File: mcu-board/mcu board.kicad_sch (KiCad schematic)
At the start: 1 part, among them U1 ESP32-S3-1

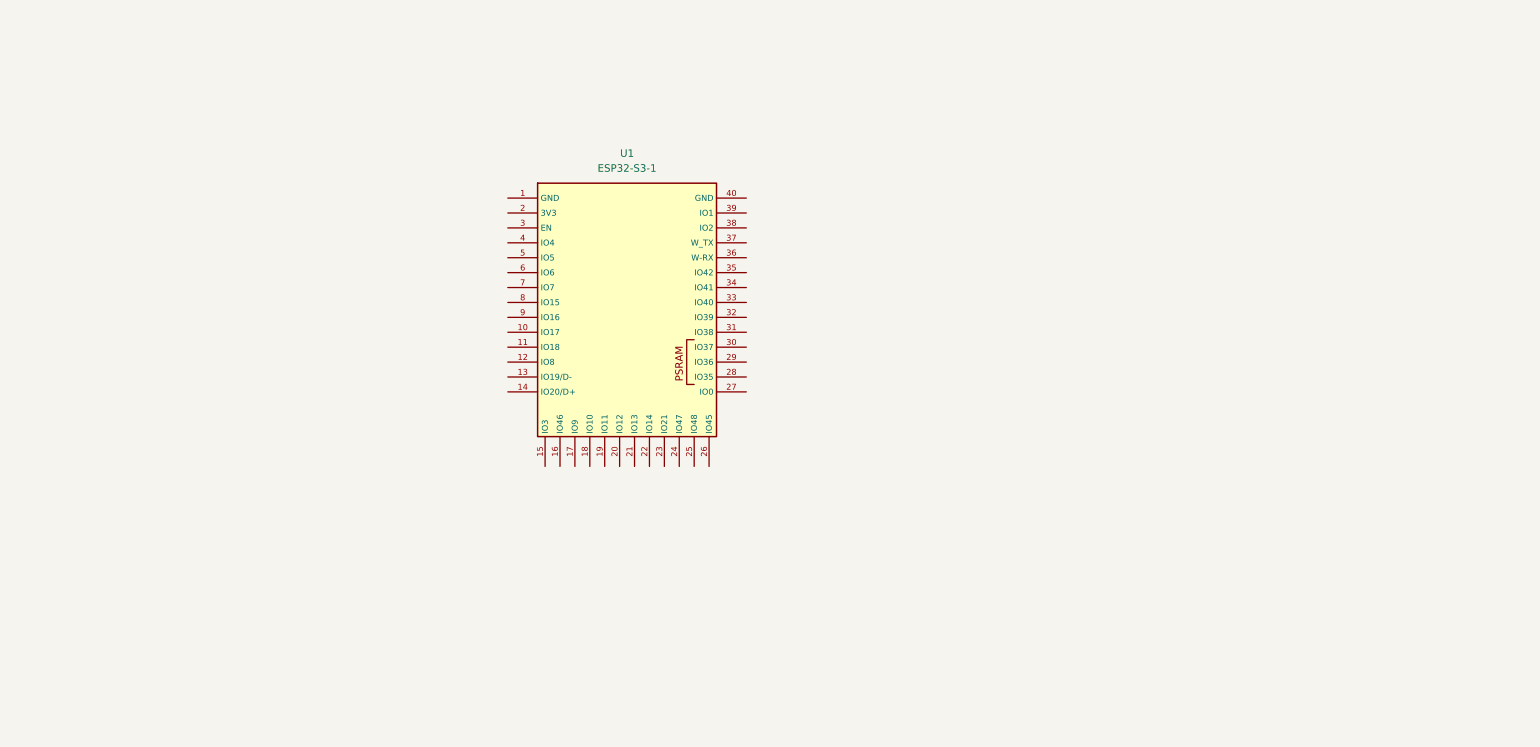
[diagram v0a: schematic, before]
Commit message: added usb-c, power, started on mcu
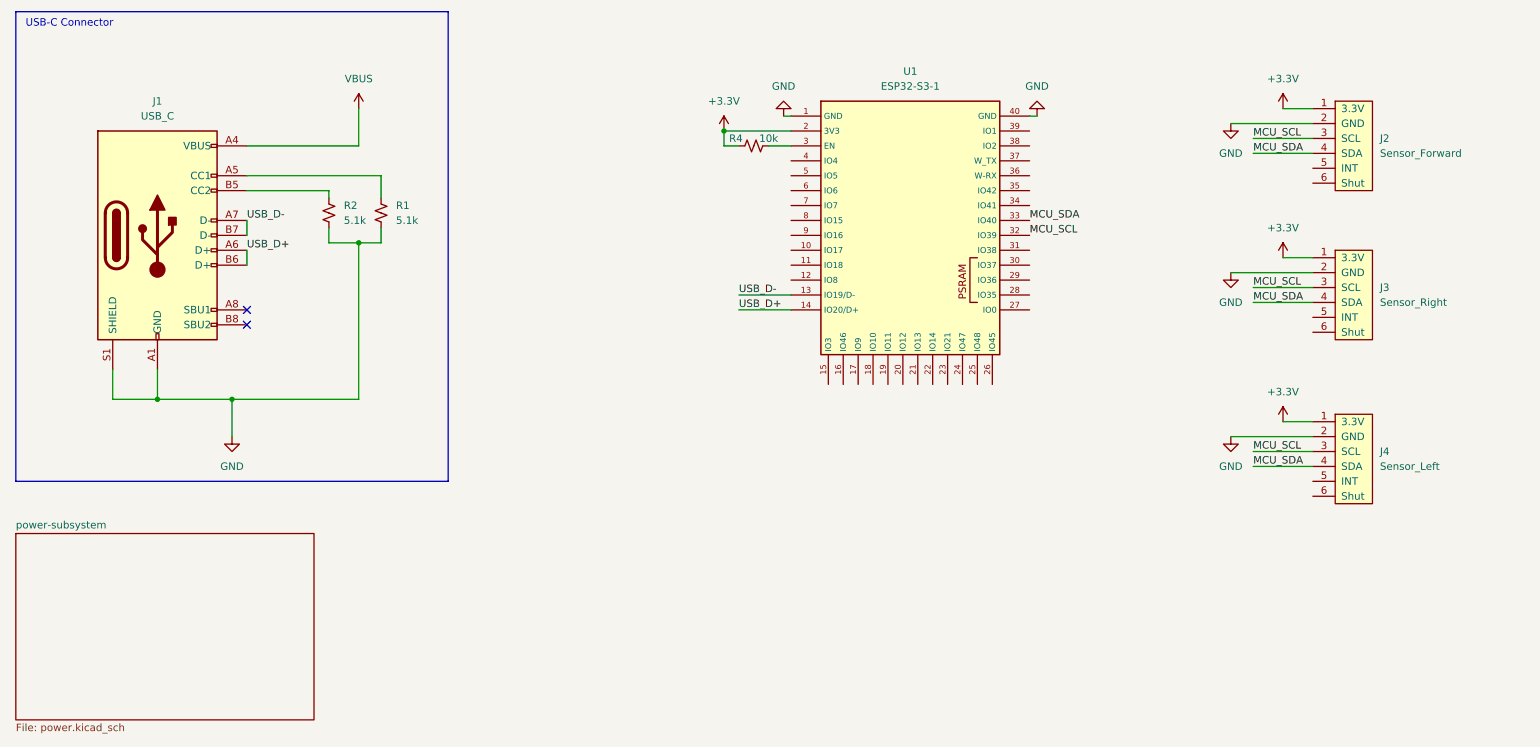
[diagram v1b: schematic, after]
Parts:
- added J1: USB_C, symbol Connector:USB_C_Receptacle_USB2.0_16P
- added J2: Sensor_Forward, EESD:1x6 Socket, symbol mouseLib:TofF breakout
- added J3: Sensor_Right, EESD:1x6 Socket, symbol mouseLib:TofF breakout
- added J4: Sensor_Left, EESD:1x6 Socket, symbol mouseLib:TofF breakout
- added R1, R2: 5.1k, symbol Device:R_Small_US
- added R4: 10k, symbol Device:R_Small_US
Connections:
- net GND: now reaches U1.1 (GND)
- net GND: now also U1.40 (GND), U1.41 (GND__1), J1.A1 (GND), J1.A12 (GND), J1.B1 (GND), J1.B12 (GND), J1.S1 (SHIELD), J2.2 (GND), J3.2 (GND), J4.2 (GND), R1.1, R2.1
- net USB_D-: now reaches U1.13 (IO19/D-)
- net USB_D-: now also J1.A7 (D-), J1.B7 (D-)
- net USB_D+: now reaches U1.14 (IO20/D+)
- net USB_D+: now also J1.A6 (D+), J1.B6 (D+)
- net +3.3V: now reaches U1.2 (3V3)
- net +3.3V: now also J2.1 (3.3V), J3.1 (3.3V), J4.1 (3.3V), R4.1
- net at U1.3 (EN): now also R4.2
- net MCU_SCL: now reaches U1.32 (IO39)
- net MCU_SCL: now also J2.3 (SCL), J3.3 (SCL), J4.3 (SCL)
- net MCU_SDA: now reaches U1.33 (IO40)
- net MCU_SDA: now also J2.4 (SDA), J3.4 (SDA), J4.4 (SDA)
- new net: J1.A5 (CC1), R1.2
- new net: J1.B5 (CC2), R2.2
- new net VBUS: J1.A4 (VBUS), J1.A9 (VBUS), J1.B4 (VBUS), J1.B9 (VBUS)
- no-connect marks 0 -> 2
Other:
- added sheet power-subsystem (power.kicad_sch)
- note added: "USB-C Connector"
- company: (none) -> Team 6.7 MHz
- title: (none) -> Mouse Board
- moved on the sheet: U1

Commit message: finished schematic(?)
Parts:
- added C7: .1u, symbol Device:C_Small
- added C8: 1u, symbol Device:C_Small
- added C9: 22u, symbol Device:C_Small
- added D4: LED, symbol Device:LED
- added J5: I2C Breakout, symbol Connector_Generic:Conn_01x04
- added M1, M2: ~, RMSmouse:gearmotorenc, symbol mouseLib:Motor
- added SW1: BOOT, symbol Switch:SW_Push
- added SW2: RESET, symbol Switch:SW_Push
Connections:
- net +3.3V: now also R4.2, C9.2, J5.2 (Pin_2); no longer R4.1
- net GND: now also C7.2, C8.2, C9.1, D4.1 (K), J5.1 (Pin_1), SW1.2, SW2.2
- net MCU_SCL: now also J5.3 (Pin_3)
- net MCU_SDA: now also J5.4 (Pin_4)
- net MCU_ENABLE: now reaches U1.3 (EN)
- net MCU_ENABLE: now also R4.1, C8.1, SW2.1; no longer R4.2
- net MCU_IO17: now reaches U1.10 (IO17)
- net MCU_IO17: now also J4.5 (INT)
- net BOOT_SEL: now reaches U1.27 (IO0)
- net BOOT_SEL: now also C7.1, SW1.1
- net at U1.35 (IO42): now also D4.2 (A)
- net MCU_IO4: now reaches U1.4 (IO4)
- net MCU_IO4: now also J4.6 (Shut)
- net MCU_IO6: now reaches U1.6 (IO6)
- net MCU_IO6: now also J2.6 (Shut)
- net MCU_IO7: now reaches U1.7 (IO7)
- net MCU_IO7: now also J3.6 (Shut)
- net MCU_IO15: now reaches U1.8 (IO15)
- net MCU_IO15: now also J2.5 (INT)
- net MCU_IO16: now reaches U1.9 (IO16)
- net MCU_IO16: now also J3.5 (INT)
- no-connect marks 2 -> 3
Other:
- note added: "blinky for testing mcu"
- moved on the sheet: J2, J3, J4, R4

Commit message: footprints
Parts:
- C7, C8: footprint (none) -> Capacitor_SMD:C_0603_1608Metric
- C9: footprint (none) -> Capacitor_SMD:C_0805_2012Metric
- J1: footprint (none) -> Connector_USB:USB_C_Receptacle_GCT_USB4105-xx-A_16P_TopMnt_Horizontal
- J5: footprint (none) -> Connector_PinSocket_2.54mm:PinSocket_1x40_P2.54mm_Vertical
- M1, M2: footprint RMSmouse:gearmotorenc -> mouseLib:gearmotorenc
- R1, R2, R4: footprint (none) -> Resistor_SMD:R_0603_1608Metric
- U1: footprint RMSmouse:450301014042 -> mouseLib:450301014042
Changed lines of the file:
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@@
 			)
 		)
-		(property "Footprint" ""
+		(property "Footprint" "Resistor_SMD:R_0603_1608Metric"
 			(at 111.76 36.83 0)
 			(effects
@@
 			)
 		)
-		(property "Footprint" "RMSmouse:450301014042"
+		(property "Footprint" "mouseLib:450301014042"
 			(at 172.72 55.88 0)
 			(effects
@@
 			)
 		)
-		(property "Footprint" ""
+		(property "Footprint" "Capacitor_SMD:C_0805_2012Metric"
 			(at 142.24 36.83 0)
 			(effects
@@
 			)
 		)
-		(property "Footprint" ""
+		(property "Footprint" "Capacitor_SMD:C_0603_1608Metric"
 			(at 114.3 59.69 0)
 			(effects
@@
 			)
 		)
-		(property "Footprint" "RMSmouse:gearmotorenc"
+		(property "Footprint" "mouseLib:gearmotorenc"
 			(at 81.28 120.65 0)
 			(effects
@@
 			)
 		)
-		(property "Footprint" ""
+		(property "Footprint" "Connector_PinSocket_2.54mm:PinSocket_1x40_P2.54mm_Vertical"
 			(at 255.27 97.79 0)
 			(effects
@@
 			)
 		)
-		(property "Footprint" ""
+		(property "Footprint" "Resistor_SMD:R_0603_1608Metric"
 			(at 82.55 54.61 0)
 			(effects
@@
 			)
 		)
-		(property "Footprint" ""
+		(property "Footprint" "Connector_USB:USB_C_Receptacle_GCT_USB4105-xx-A_16P_TopMnt_Horizontal"
 			(at 48.26 58.42 0)
 			(effects
@@
 			)
 		)
-		(property "Footprint" ""
+		(property "Footprint" "Resistor_SMD:R_0603_1608Metric"
 			(at 73.66 54.61 0)
 			(effects
@@
 			)
 		)
-		(property "Footprint" "RMSmouse:gearmotorenc"
+		(property "Footprint" "mouseLib:gearmotorenc"
 			(at 81.28 113.03 0)
 			(effects
@@
 			)
 		)
-		(property "Footprint" ""
+		(property "Footprint" "Capacitor_SMD:C_0603_1608Metric"
 			(at 114.3 80.01 0)
 			(effects

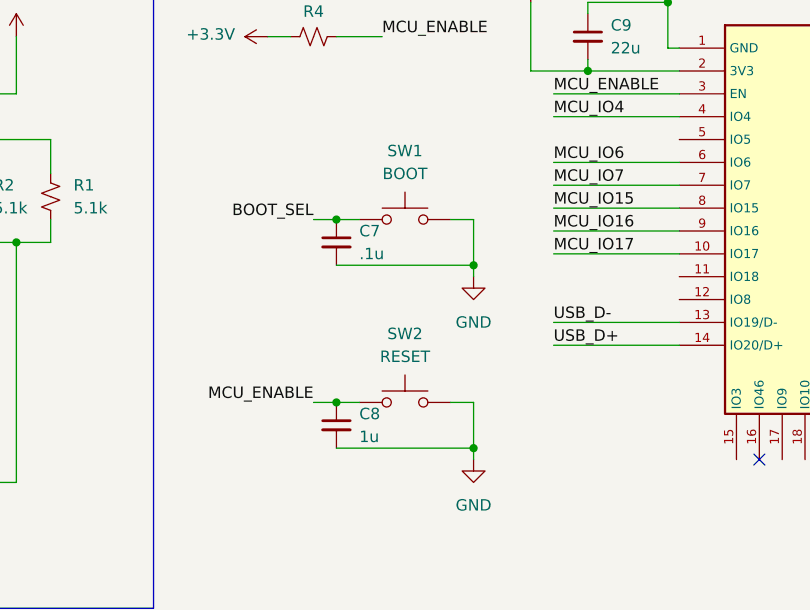
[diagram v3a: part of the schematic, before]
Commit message: pcb routed
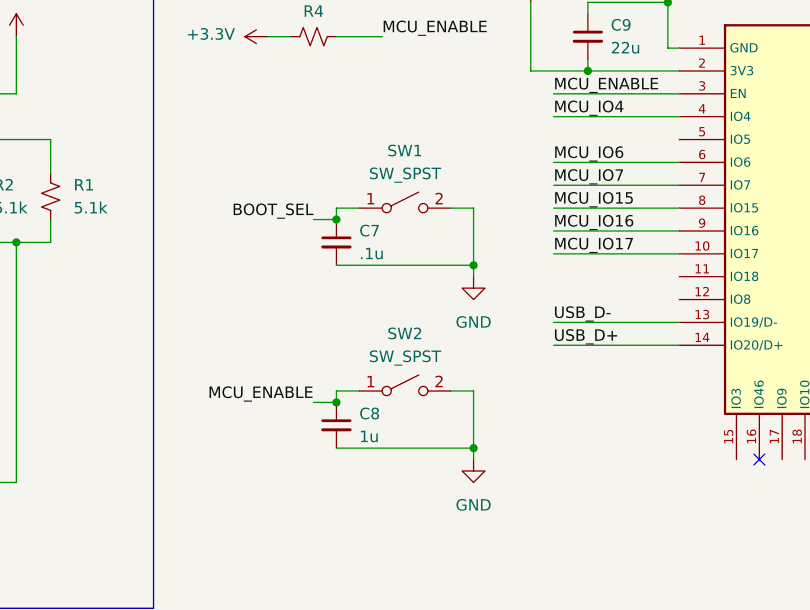
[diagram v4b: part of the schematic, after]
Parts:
- removed SW1: BOOT, symbol Switch:SW_Push
- removed SW2: RESET, symbol Switch:SW_Push
- added SW1, SW2: SW_SPST, Button_Switch_THT:SW_TH_Tactile_Omron_B3F-100x, symbol Switch:SW_SPST
- D4: footprint (none) -> LED_SMD:LED_0603_1608Metric
- J2, J3, J4: footprint EESD:1x6 Socket -> Connector_PinSocket_2.54mm:PinSocket_1x06_P2.54mm_Vertical
- J5: footprint Connector_PinSocket_2.54mm:PinSocket_1x40_P2.54mm_Vertical -> Connector_PinSocket_2.54mm:PinSocket_1x04_P2.54mm_Vertical
- U1: footprint mouseLib:450301014042 -> mouseLib:ESP32-S3-1-WROOM_1
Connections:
- net BOOT_SEL: now also SW1.1 (A)
- net GND: now also SW1.2 (B), SW2.2 (B)
- net MCU_ENABLE: now also SW2.1 (A)
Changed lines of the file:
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@@
 	(wire
 		(pts
-			(xy 129.54 82.55) (xy 129.54 77.47)
+			(xy 129.54 82.55) (xy 129.54 76.2)
 		)
 		(stroke
@@
 	(wire
 		(pts
-			(xy 114.3 57.15) (xy 116.84 57.15)
+			(xy 114.3 55.88) (xy 116.84 55.88)
 		)
 		(stroke
@@
 	(wire
 		(pts
+			(xy 114.3 76.2) (xy 114.3 77.47)
+		)
+		(stroke
+			(width 0)
+			(type default)
+		)
+	)
+	(wire
+		(pts
 			(xy 82.55 52.07) (xy 82.55 48.26)
 		)
@@
 	(wire
 		(pts
-			(xy 129.54 77.47) (xy 127 77.47)
+			(xy 129.54 76.2) (xy 127 76.2)
 		)
 		(stroke
@@
 	(wire
 		(pts
-			(xy 129.54 57.15) (xy 129.54 62.23)
+			(xy 129.54 55.88) (xy 129.54 62.23)
 		)
 		(stroke
@@
 	(wire
 		(pts
-			(xy 129.54 57.15) (xy 127 57.15)
+			(xy 129.54 55.88) (xy 127 55.88)
 		)
 		(stroke
@@
 	(wire
 		(pts
-			(xy 114.3 77.47) (xy 116.84 77.47)
+			(xy 114.3 76.2) (xy 116.84 76.2)
 		)
 		(stroke
@@
 	(wire
 		(pts
+			(xy 114.3 55.88) (xy 114.3 57.15)
+		)
+		(stroke
+			(width 0)
+			(type default)
+		)
+	)
+	(wire
+		(pts
 			(xy 193.04 50.8) (xy 204.47 50.8)
 		)
@@
 	)
 	(symbol
+		(lib_id "Switch:SW_SPST")
+		(at 121.92 55.88 0)
+		(unit 1)
+		(exclude_from_sim no)
+		(in_bom yes)
+		(on_board yes)
+		(dnp no)
+		(fields_autoplaced yes)
+		(property "Reference" "SW1"
+			(at 121.92 49.53 0)
+			(effects
+				(font
+					(size 1.27 1.27)
+				)
+			)
+		)
+		(property "Value" "SW_SPST"
+			(at 121.92 52.07 0)
+			(effects
+				(font
+					(size 1.27 1.27)
+				)
+			)
+		)
+		(property "Footprint" "Button_Switch_THT:SW_TH_Tactile_Omron_B3F-100x"
+			(at 121.92 55.88 0)
+			(effects
+				(font
+					(size 1.27 1.27)
+				)
+				(hide yes)
+			)
+		)
+		(property "Datasheet" "~"
+			(at 121.92 55.88 0)
+			(effects
+				(font
+					(size 1.27 1.27)
+				)
+				(hide yes)
+			)
+		)
+		(property "Description" "Single Pole Single Throw (SPST) switch"
+			(at 121.92 55.88 0)
+			(effects
+				(font
+					(size 1.27 1.27)
+				)
+				(hide yes)
+			)
+		)
+		(pin "1"
+		)
+		(pin "2"
+		)
+		(instances
+			(project "mcu board"
+				(path "/e926887c-cd26-4f47-be51-3352b14f6743"
+					(reference "SW1")
+					(unit 1)
+				)
+			)
+		)
+	)
+	(symbol
 		(lib_id "power:+3.3V")
 		(at 240.03 97.79 90)
@@
 			)
 		)
-		(property "Footprint" "mouseLib:450301014042"
+		(property "Footprint" "mouseLib:ESP32-S3-1-WROOM_1"
 			(at 172.72 55.88 0)
 			(effects
@@
 	)
 	(symbol
-		(lib_id "Switch:SW_Push")
-		(at 121.92 57.15 0)
-		(unit 1)
-		(exclude_from_sim no)
-		(in_bom yes)
-		(on_board yes)
-		(dnp no)
-		(fields_autoplaced yes)
-		(property "Reference" "SW1"
-			(at 121.92 49.53 0)
-			(effects
-				(font
-					(size 1.27 1.27)
-				)
-			)
-		)
-		(property "Value" "BOOT"
-			(at 121.92 52.07 0)
-			(effects
-				(font
-					(size 1.27 1.27)
-				)
-			)
-		)
-		(property "Footprint" ""
-			(at 121.92 52.07 0)
-			(effects
-				(font
-					(size 1.27 1.27)
-				)
-				(hide yes)
-			)
-		)
-		(property "Datasheet" "~"
-			(at 121.92 52.07 0)
-			(effects
-				(font
-					(size 1.27 1.27)
-				)
-				(hide yes)
-			)
-		)
-		(property "Description" "Push button switch, generic, two pins"
-			(at 121.92 57.15 0)
-			(effects
-				(font
-					(size 1.27 1.27)
-				)
-				(hide yes)
-			)
-		)
-		(pin "2"
-		)
-		(pin "1"
-		)
-		(instances
-			(project ""
-				(path "/e926887c-cd26-4f47-be51-3352b14f6743"
-					(reference "SW1")
-					(unit 1)
-				)
-			)
-		)
-	)
-	(symbol
 		(lib_id "power:GND")
 		(at 240.03 95.25 270)
@@
 			)
 		)
-		(property "Footprint" ""
+		(property "Footprint" "LED_SMD:LED_0603_1608Metric"
 			(at 208.28 50.8 0)
 			(effects
@@
 			)
 		)
-		(property "Footprint" "Connector_PinSocket_2.54mm:PinSocket_1x40_P2.54mm_Vertical"
+		(property "Footprint" "Connector_PinSocket_2.54mm:PinSocket_1x04_P2.54mm_Vertical"
 			(at 255.27 97.79 0)
 			(effects
@@
 			)
 		)
-		(property "Footprint" "EESD:1x6 Socket"
+		(property "Footprint" "Connector_PinSocket_2.54mm:PinSocket_1x06_P2.54mm_Vertical"
 			(at 254.508 45.72 0)
 			(effects
@@
 			)
 		)
-		(property "Footprint" "EESD:1x6 Socket"
+		(property "Footprint" "Connector_PinSocket_2.54mm:PinSocket_1x06_P2.54mm_Vertical"
 			(at 254.508 67.31 0)
 			(effects
@@
 	)
 	(symbol
+		(lib_id "Switch:SW_SPST")
+		(at 121.92 76.2 0)
+		(unit 1)
+		(exclude_from_sim no)
+		(in_bom yes)
+		(on_board yes)
+		(dnp no)
+		(fields_autoplaced yes)
+		(property "Reference" "SW2"
+			(at 121.92 69.85 0)
+			(effects
+				(font
+					(size 1.27 1.27)
+				)
+			)
+		)
+		(property "Value" "SW_SPST"
+			(at 121.92 72.39 0)
+			(effects
+				(font
+					(size 1.27 1.27)
+				)
+			)
+		)
+		(property "Footprint" "Button_Switch_THT:SW_TH_Tactile_Omron_B3F-100x"
+			(at 121.92 76.2 0)
+			(effects
+				(font
+					(size 1.27 1.27)
+				)
+				(hide yes)
+			)
+		)
+		(property "Datasheet" "~"
+			(at 121.92 76.2 0)
+			(effects
+				(font
+					(size 1.27 1.27)
+				)
+				(hide yes)
+			)
+		)
+		(property "Description" "Single Pole Single Throw (SPST) switch"
+			(at 121.92 76.2 0)
+			(effects
+				(font
+					(size 1.27 1.27)
+				)
+				(hide yes)
+			)
+		)
+		(pin "1"
+		)
+		(pin "2"
+		)
+		(instances
+			(project ""
+				(path "/e926887c-cd26-4f47-be51-3352b14f6743"
+					(reference "SW2")
+					(unit 1)
+				)
+			)
+		)
+	)
+	(symbol
 		(lib_id "power:GND")
 		(at 234.95 33.02 0)
@@
 	)
 	(symbol
-		(lib_id "Switch:SW_Push")
-		(at 121.92 77.47 0)
-		(unit 1)
-		(exclude_from_sim no)
-		(in_bom yes)
-		(on_board yes)
-		(dnp no)
-		(fields_autoplaced yes)
-		(property "Reference" "SW2"
-			(at 121.92 69.85 0)
-			(effects
-				(font
-					(size 1.27 1.27)
-				)
-			)
-		)
-		(property "Value" "RESET"
-			(at 121.92 72.39 0)
-			(effects
-				(font
-					(size 1.27 1.27)
-				)
-			)
-		)
-		(property "Footprint" ""
-			(at 121.92 72.39 0)
-			(effects
-				(font
-					(size 1.27 1.27)
-				)
-				(hide yes)
-			)
-		)
-		(property "Datasheet" "~"
-			(at 121.92 72.39 0)
-			(effects
-				(font
-					(size 1.27 1.27)
-				)
-				(hide yes)
-			)
-		)
-		(property "Description" "Push button switch, generic, two pins"
-			(at 121.92 77.47 0)
-			(effects
-				(font
-					(size 1.27 1.27)
-				)
-				(hide yes)
-			)
-		)
-		(pin "2"
-		)
-		(pin "1"
-		)
-		(instances
-			(project "mcu board"
-				(path "/e926887c-cd26-4f47-be51-3352b14f6743"
-					(reference "SW2")
-					(unit 1)
-				)
-			)
-		)
-	)
-	(symbol
 		(lib_id "Device:C_Small")
 		(at 114.3 80.01 0)
@@
 			)
 		)
-		(property "Footprint" "EESD:1x6 Socket"
+		(property "Footprint" "Connector_PinSocket_2.54mm:PinSocket_1x06_P2.54mm_Vertical"
 			(at 254.508 24.13 0)
 			(effects
